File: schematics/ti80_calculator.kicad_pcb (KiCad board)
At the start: 2 copper layers, 66 x 106.8 mm, 116 parts, among them J10 0, J13 0, J14 0Ω, J15 0Ω, J16 0, J17 0Ω, J18 0, J5 0Ω, J7 0Ω, J8 0, J9 0Ω, Q2 LG, Q3 LG, Q4 RIQ, SW1 Slide Switch, SW10 CLEAR, SW11 VARS, SW12 PRGM, SW13 FRAC, SW14 MATH, SW15 MODE, SW17 ^, SW18 TAN, SW19 COS, SW2 ON, SW20 SIN, SW21 x⁻¹, SW22 2nd, SW24 ÷, SW25 ), SW26 (, SW27 ,, SW28 x², SW29 Y=, SW30 ▲, SW31 ×, SW32 9, SW33 8, SW34 7, SW35 LOG, SW36 WINDOW, SW37 ►, SW38 -, SW39 6, SW40 5, SW41 4, SW42 LN, SW43 ZOOM, SW44 ◄, SW45 +, SW46 3, SW47 2, SW48 1, SW49 STO►, SW5 STAT, SW50 TRACE, SW51 ▼, SW52 ENTER, SW53 (-), SW54 •, SW55 0, SW57 GRAPH, SW6 X,T, SW7 ALPHA, SW8 DEL, U1 T6M53A, U2 LH5359, U3 SRM2264, U4 T6B79

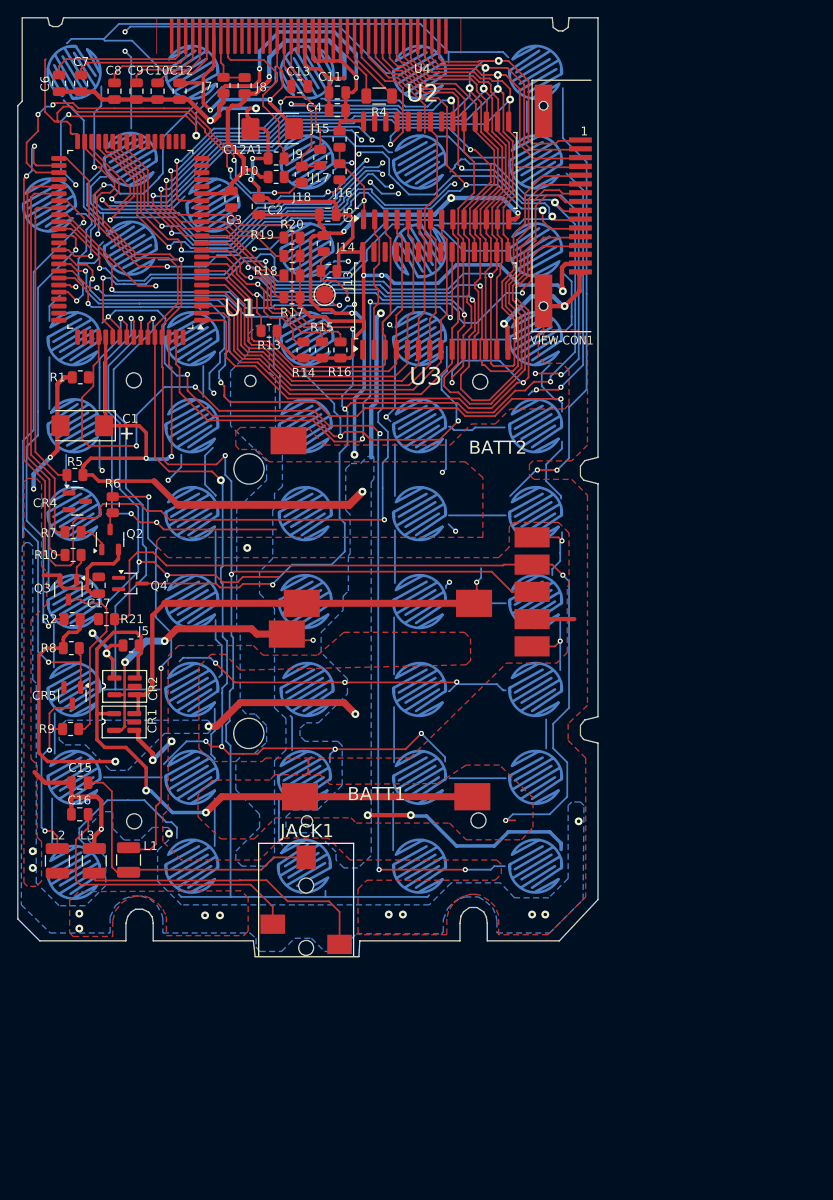
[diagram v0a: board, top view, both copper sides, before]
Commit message: Make PCB layout orientation portrait and add title and date
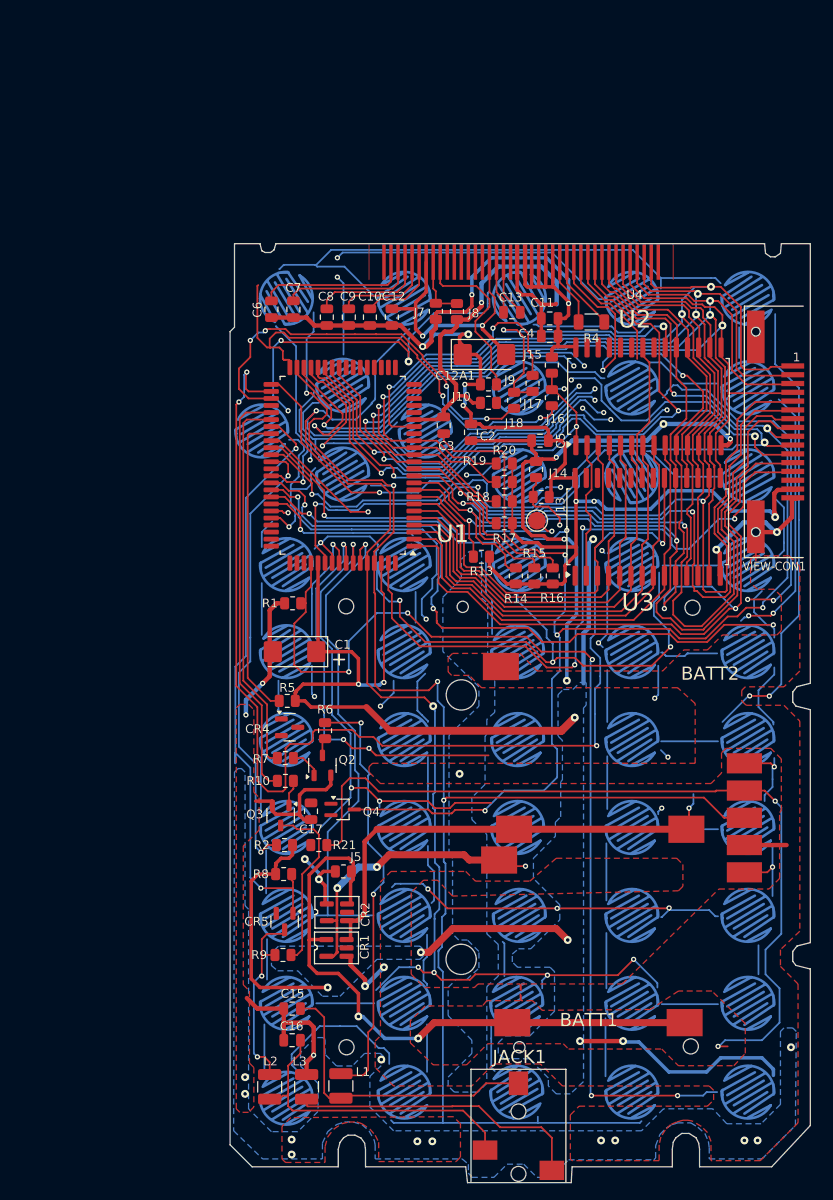
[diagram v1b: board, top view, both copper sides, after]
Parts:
- moved L1 35.3 mm to (86.8, 171.4)
- moved R6 35.3 mm to (85.0, 131.0)
- moved R8 35.3 mm to (80.2, 147.3)
- moved SW52 35.3 mm to (80.5, 172.8)
- moved C1 35.3 mm to (81.5, 122.0)
- moved C11 35.3 mm to (110.5, 84.1)
- moved C13 35.3 mm to (106.2, 83.4)
- moved C3 35.3 mm to (98.5, 96.2)
- moved C4 35.3 mm to (110.5, 86.1)
- moved C5 35.3 mm to (109.4, 98.0)
- moved C8 35.3 mm to (85.2, 84.0)
- moved C9 35.3 mm to (87.7, 84.0)
- moved J15 35.3 mm to (110.8, 89.4)
- moved J16 35.3 mm to (110.8, 93.1)
- moved J8 35.3 mm to (100.0, 83.3)
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
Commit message: Update key footprint and redo keypad routing
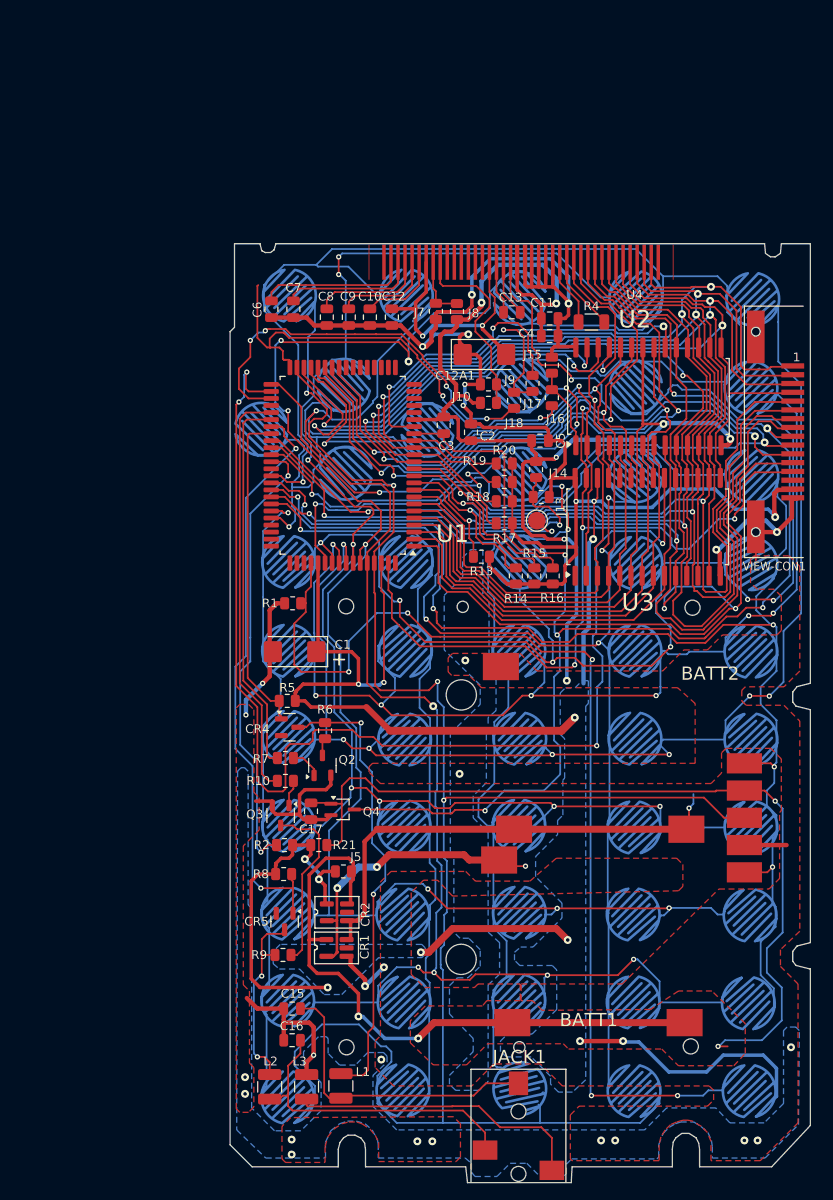
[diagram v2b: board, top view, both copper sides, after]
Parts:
- moved SW44 18.9 mm to (96.6, 96.8), turned to 75 degrees
- moved SW37 18.7 mm to (77.7, 96.7), turned to 75 degrees
- moved SW55 13.4 mm to (120.1, 172.0), turned to -15 degrees
- moved SW54 12.8 mm to (107.1, 171.7), turned to -45 degrees
- moved SW29 0.56 mm to (133.6, 81.9), turned to -15 degrees
- moved SW13 0.49 mm to (120.3, 111.9), turned to -15 degrees
- moved SW36 0.46 mm to (120.3, 81.7), turned to 165 degrees
- moved SW57 0.46 mm to (80.9, 81.5), turned to -15 degrees
- moved SW15 0.46 mm to (120.3, 91.9), turned to -105 degrees
- moved SW6 0.46 mm to (120.3, 102.0), turned to 80 degrees
- moved SW7 0.45 mm to (133.5, 102.0), turned to 165 degrees
- moved SW24 0.39 mm to (80.8, 131.7), turned to -15 degrees
- moved SW10 0.39 mm to (80.8, 111.8), turned to -15 degrees
- moved SW11 0.39 mm to (94.2, 111.8), turned to 165 degrees
- moved SW47 0.39 mm to (107.0, 161.7), turned to -15 degrees
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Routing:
- net (no net): track 601.5 -> 0.00 mm, vias 28 -> 0
- net COL6: track 23.3 -> 153.5 mm
- net ROW2: track 55.9 -> 172.4 mm, vias 1 -> 7
- net ROW3: track 56.6 -> 170.5 mm, vias 3 -> 8
- net ROW5: track 13.7 -> 122.7 mm, vias 1 -> 7
- net COL4: track 32.2 -> 126.3 mm, vias 2 -> 5
- net ROW4: track 46.3 -> 135.4 mm, vias 3 -> 7
- net COL3: track 38.9 -> 114.2 mm, vias 1 -> 3
- net COL1: track 2.01 -> 72.5 mm
- net COL2: track 18.4 -> 86.9 mm
- net ROW6: track 74.9 -> 140.2 mm, vias 4 -> 6
- net COL5: track 102.7 -> 149.5 mm
- net ROW7: track 48.3 -> 91.4 mm, vias 2 -> 5
- net ROW0: track 179.1 -> 217.6 mm
- net COL0: track 19.4 -> 53.0 mm
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
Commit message: Add test points for power and keypad
- Add battery test points on front and back of PCB
- Add test points for row and columns on keypad side of PCB
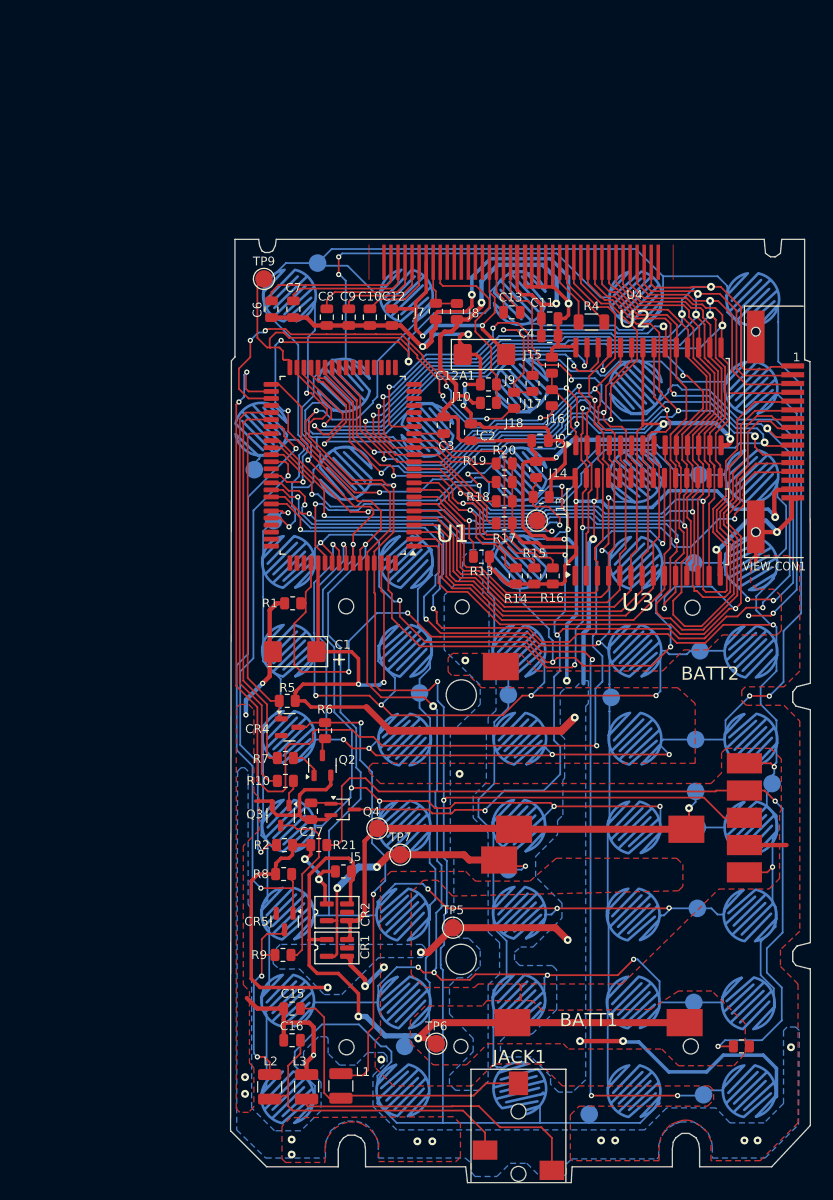
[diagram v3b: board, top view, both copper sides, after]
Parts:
- added J1: Open, Resistor_SMD:R_0805_2012Metric, F.Cu at (132.3, 166.9)
- added TP10: Pin 50 Test Point, TestPoint:TestPoint_Pad_D2.0mm, B.Cu at (76.9, 101.3)
- added TP11: Pin 50 Test Point, TestPoint:TestPoint_Pad_D2.0mm, B.Cu at (79.1, 107.1)
- added TP12: Pin 50 Test Point, TestPoint:TestPoint_Pad_D2.0mm, B.Cu at (95.7, 126.7)
- added TP13: Pin 50 Test Point, TestPoint:TestPoint_Pad_D2.0mm, B.Cu at (105.8, 126.9)
- added TP14: Pin 50 Test Point, TestPoint:TestPoint_Pad_D2.0mm, B.Cu at (117.5, 127.2)
- added TP15: Pin 50 Test Point, TestPoint:TestPoint_Pad_D2.0mm, B.Cu at (135.8, 137.0)
- added TP16: Pin 50 Test Point, TestPoint:TestPoint_Pad_D2.0mm, B.Cu at (84.1, 77.8)
- added TP17: Pin 50 Test Point, TestPoint:TestPoint_Pad_D2.0mm, B.Cu at (127.5, 101.9)
- added TP18: Pin 50 Test Point, TestPoint:TestPoint_Pad_D2.0mm, B.Cu at (126.9, 111.9)
- added TP19: Pin 50 Test Point, TestPoint:TestPoint_Pad_D2.0mm, B.Cu at (127.6, 121.9)
- added TP2: Pin 50 Test Point, TestPoint:TestPoint_Pad_D2.0mm, B.Cu at (105.8, 146.8)
- added TP20: Pin 50 Test Point, TestPoint:TestPoint_Pad_D2.0mm, B.Cu at (127.1, 132.0)
- added TP21: Pin 50 Test Point, TestPoint:TestPoint_Pad_D2.0mm, B.Cu at (127.3, 142.0)
- added TP22: Pin 50 Test Point, TestPoint:TestPoint_Pad_D2.0mm, B.Cu at (127.3, 151.2)
- added TP23: Pin 50 Test Point, TestPoint:TestPoint_Pad_D2.0mm, B.Cu at (126.9, 161.9)
- added TP24: Pin 50 Test Point, TestPoint:TestPoint_Pad_D2.0mm, B.Cu at (115.0, 174.6)
- added TP25: Pin 50 Test Point, TestPoint:TestPoint_Pad_D2.0mm, B.Cu at (128.0, 172.4)
- added TP3: Pin 50 Test Point, TestPoint:TestPoint_Pad_D2.0mm, B.Cu at (94.0, 166.9)
- added TP4: Pin 50 Test Point, TestPoint:TestPoint_Pad_D2.0mm, B.Cu at (127.1, 137.9)
- added TP5: Pin 50 Test Point, TestPoint:TestPoint_Pad_D2.0mm, F.Cu at (99.5, 153.4)
- added TP6: Pin 50 Test Point, TestPoint:TestPoint_Pad_D2.0mm, F.Cu at (97.6, 166.6)
- added TP7: Pin 50 Test Point, TestPoint:TestPoint_Pad_D2.0mm, F.Cu at (93.5, 145.1)
- added TP8: Pin 50 Test Point, TestPoint:TestPoint_Pad_D2.0mm, F.Cu at (90.9, 142.1)
- added TP9: Pin 50 Test Point, TestPoint:TestPoint_Pad_D2.0mm, F.Cu at (78.0, 79.6)
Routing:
- net ROW5: track 122.7 -> 118.5 mm
- net COL5: track 149.5 -> 153.3 mm
- net Net-(BATT1-+): track 72.1 -> 75.6 mm
- net GND: track 228.5 -> 231.3 mm
- net Net-(BATT1--): track 34.5 -> 36.7 mm
- net COL0: track 53.0 -> 54.9 mm
- net ROW6: track 140.2 -> 141.7 mm
- net A15: track 53.1 -> 54.1 mm
- net ROW2: track 172.4 -> 173.3 mm
- net ROW3: track 170.5 -> 169.6 mm
- net ROW0: track 217.6 -> 218.3 mm
- net ROW1: track 180.1 -> 179.4 mm
- net Net-(J1-B): track 98.8 -> 99.5 mm
- net ROW4: track 135.4 -> 136.0 mm
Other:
- board size 66 x 106.8 mm -> 66 x 107.3 mm

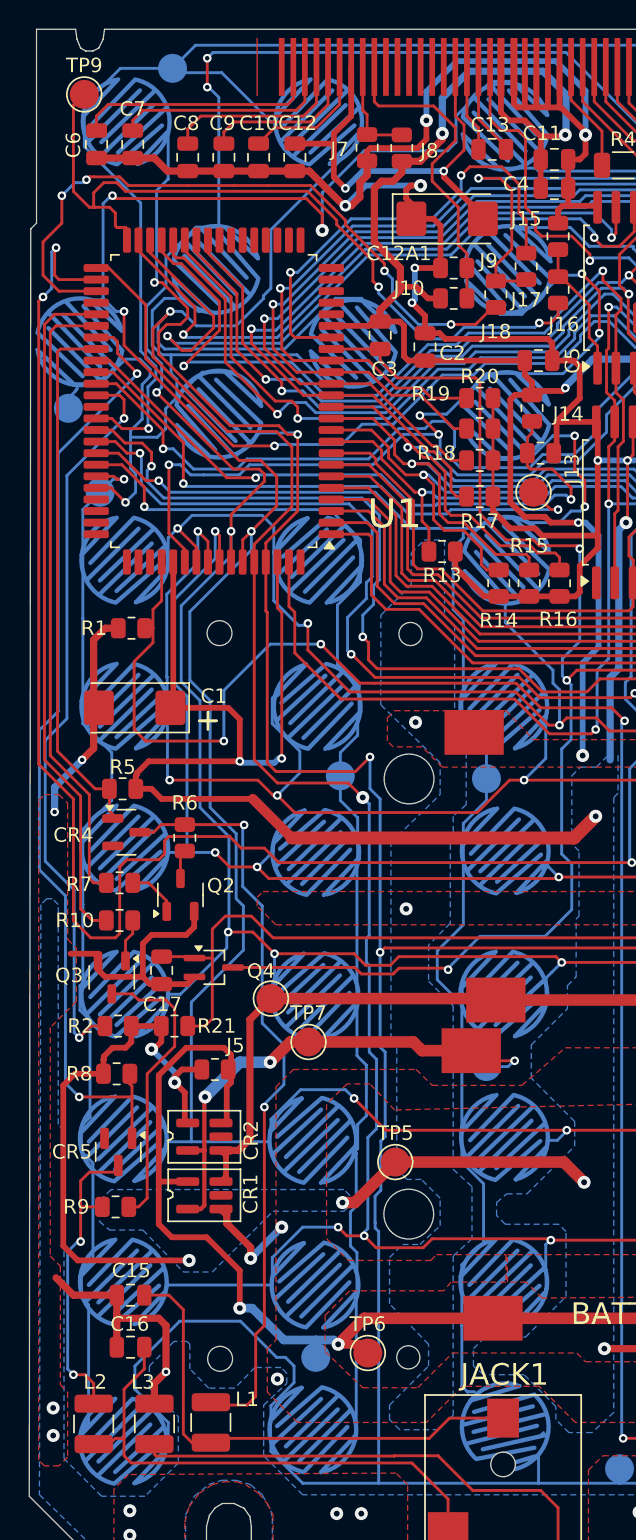
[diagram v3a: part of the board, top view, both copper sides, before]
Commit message: Change inductor package from 1210 to 1008 and hide test point silkscreens
- 1008 is likely better package size for unpopulated graph link inductors
- Remove the test point "TP" silkscreen labels
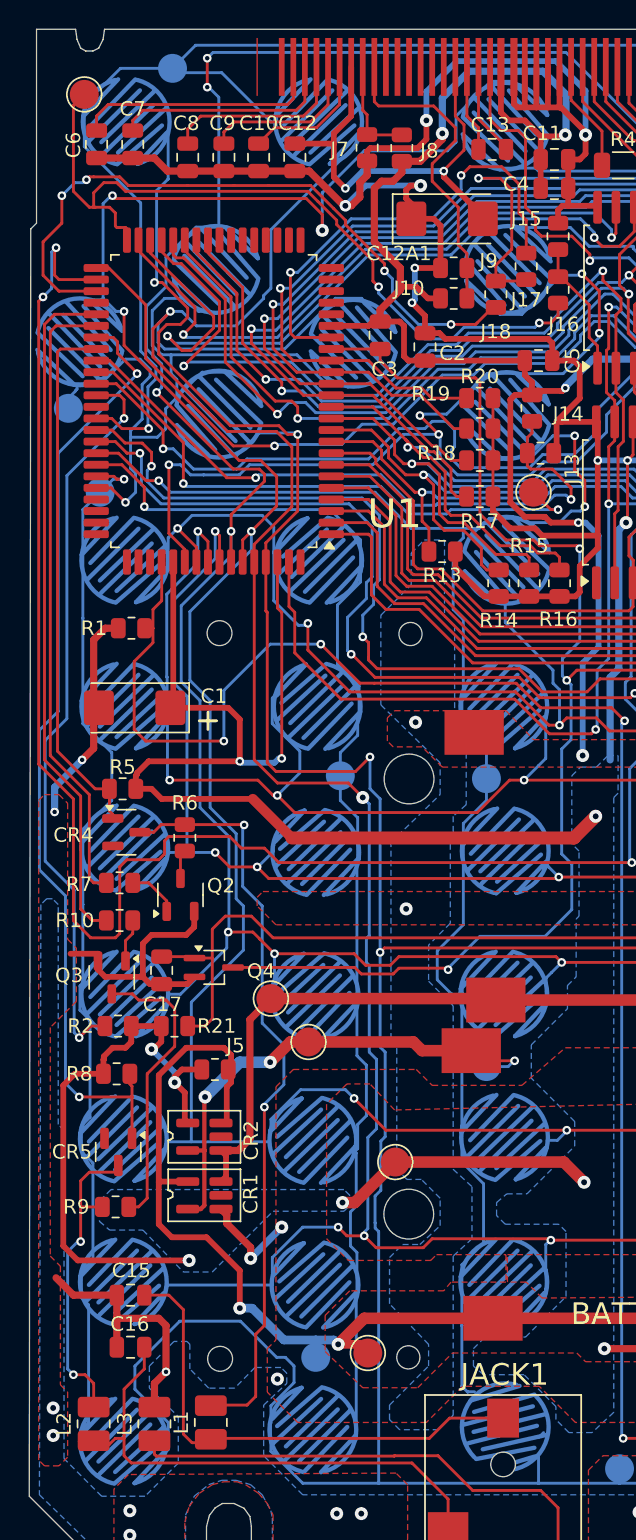
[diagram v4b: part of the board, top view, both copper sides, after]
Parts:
- L1, L2, L3: footprint Inductor_SMD:L_1210_3225Metric -> Inductor_SMD:L_1008_2520Metric_Pad1.43x2.20mm_HandSolder
